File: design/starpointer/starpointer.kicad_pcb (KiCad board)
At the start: 2 copper layers, 82.1 x 22.5 mm, 38 parts, among them J1 2.54mm Header, J2 2.54mm Header, J3 XM7D-0512, M1 ADXL345 MODULE, M2 HMC5883L MODULE, U1 STM32F103C8T6, U2 USBLC6-2SC6, U3 RT9193-33GB, Y1 32.768kHz, Y2 8.00MHz

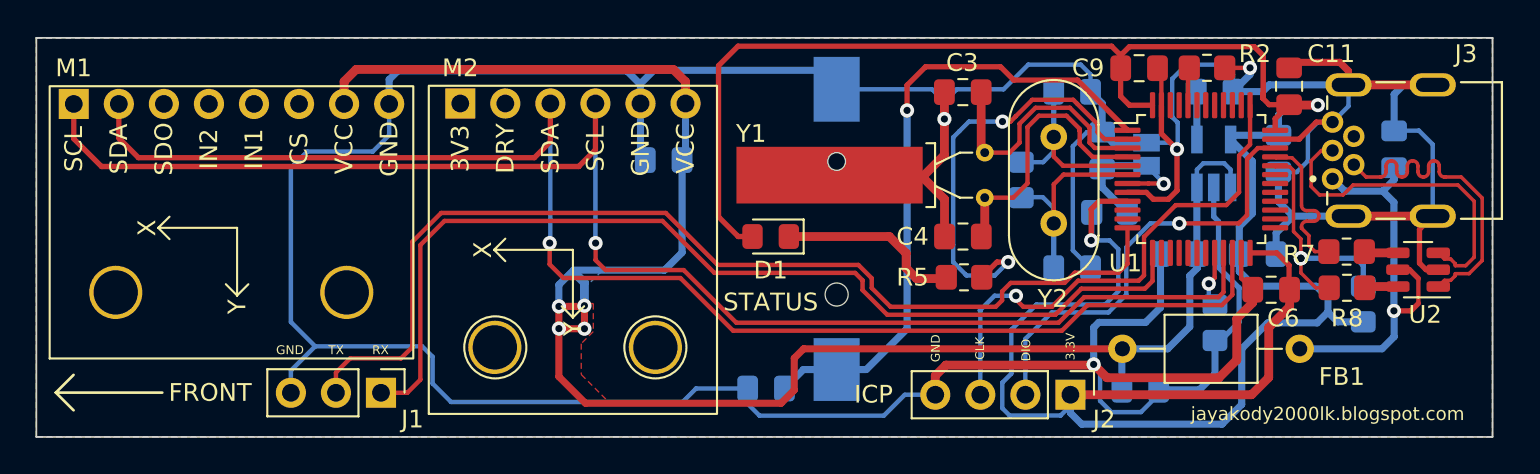
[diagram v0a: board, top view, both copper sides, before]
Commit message: Fix USB connection issue due to the missing pull-up in USB-D+ line.
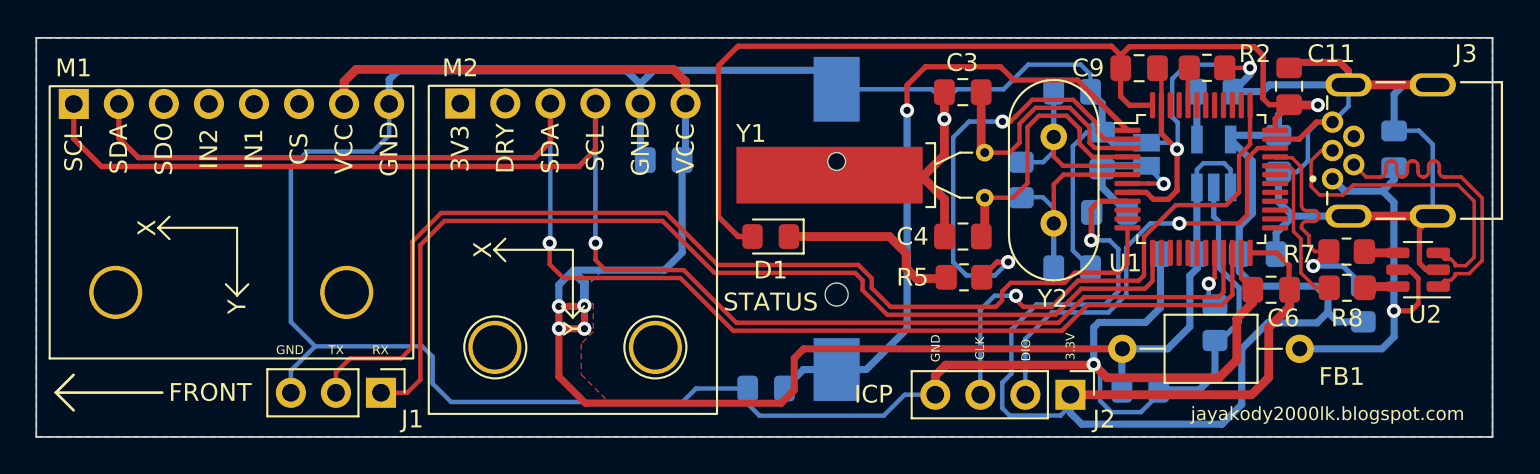
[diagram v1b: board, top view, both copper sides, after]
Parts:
- added G***: LOGO, starpointer:pcbway-logo-5mm, B.Cu at (119.1, 108.2)
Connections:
- R6 pad 2: /USB-D- -> /USB-D+
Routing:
- net /USB-D-: track 14.0 -> 9.10 mm, vias 2 -> 0
- net /USB-D+: track 9.50 -> 14.3 mm, vias 0 -> 1
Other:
- board text added: "REV 1.1"
- board text added: "Sponsored by"
- board text removed: "REV 1.0"
